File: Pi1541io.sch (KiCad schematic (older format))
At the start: 22 parts, among them J1 IEC1, J2 IEC2, J3 IEC3, J4 ExtSpkr, P1 Conn_02x20_Odd_Even, SW1 SW_Push, SW2 SW_Push, SW3 SW_Push, SW4 SW_Push, SW5 SW_Push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

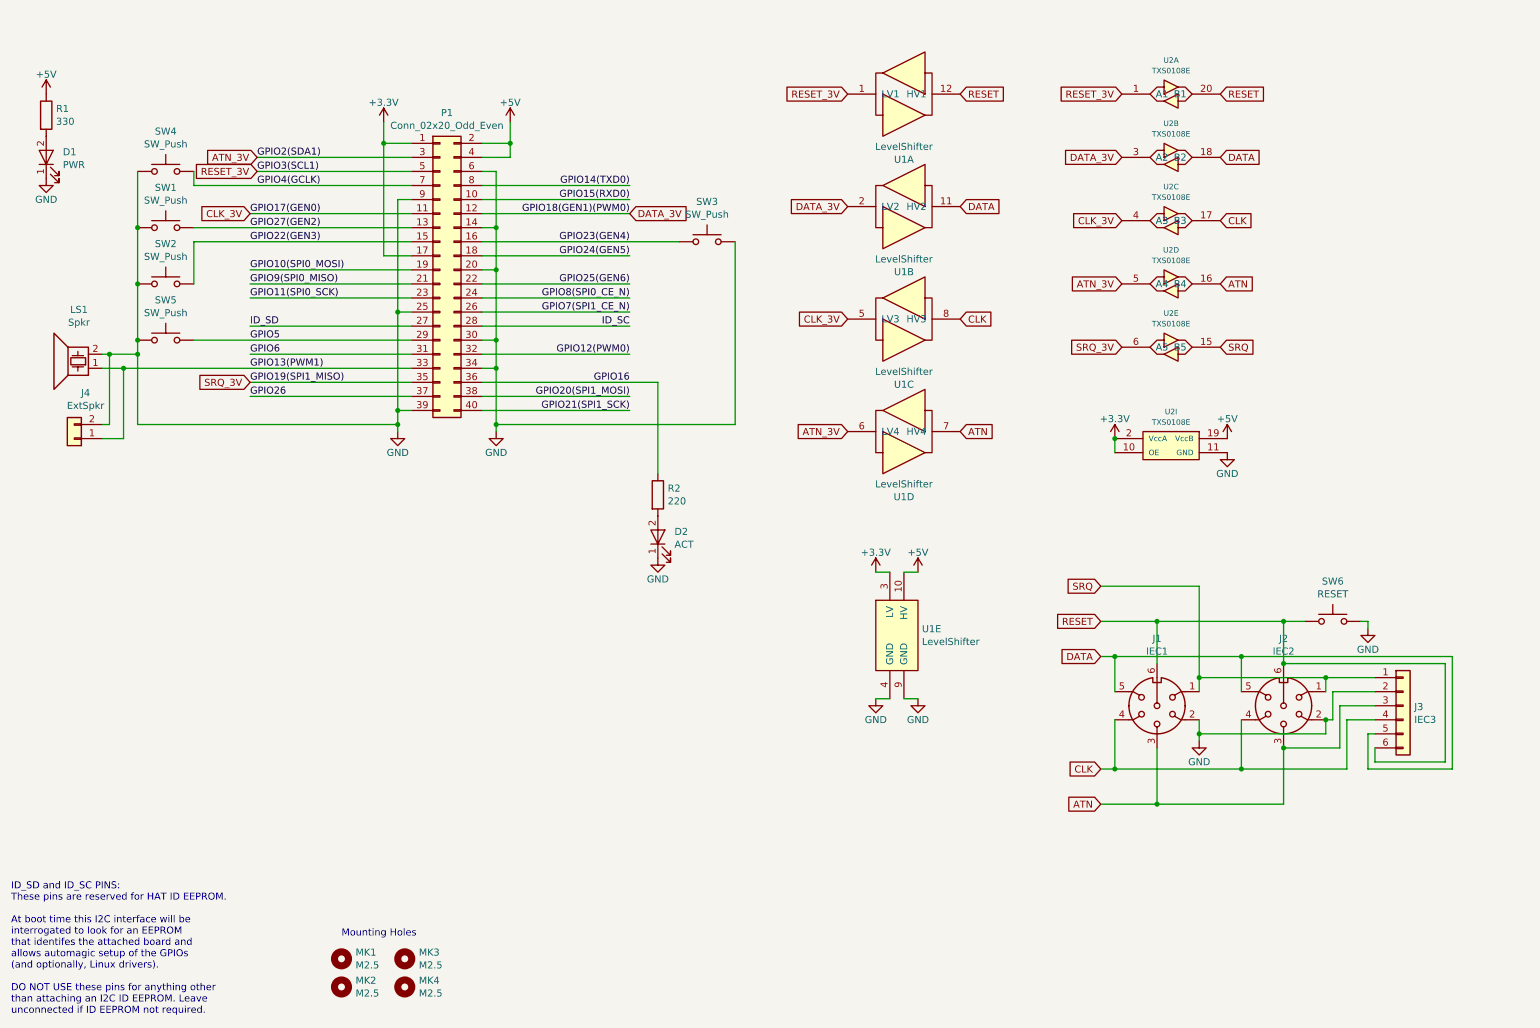
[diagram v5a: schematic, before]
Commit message: Added 7406 driver for outgoing signals.
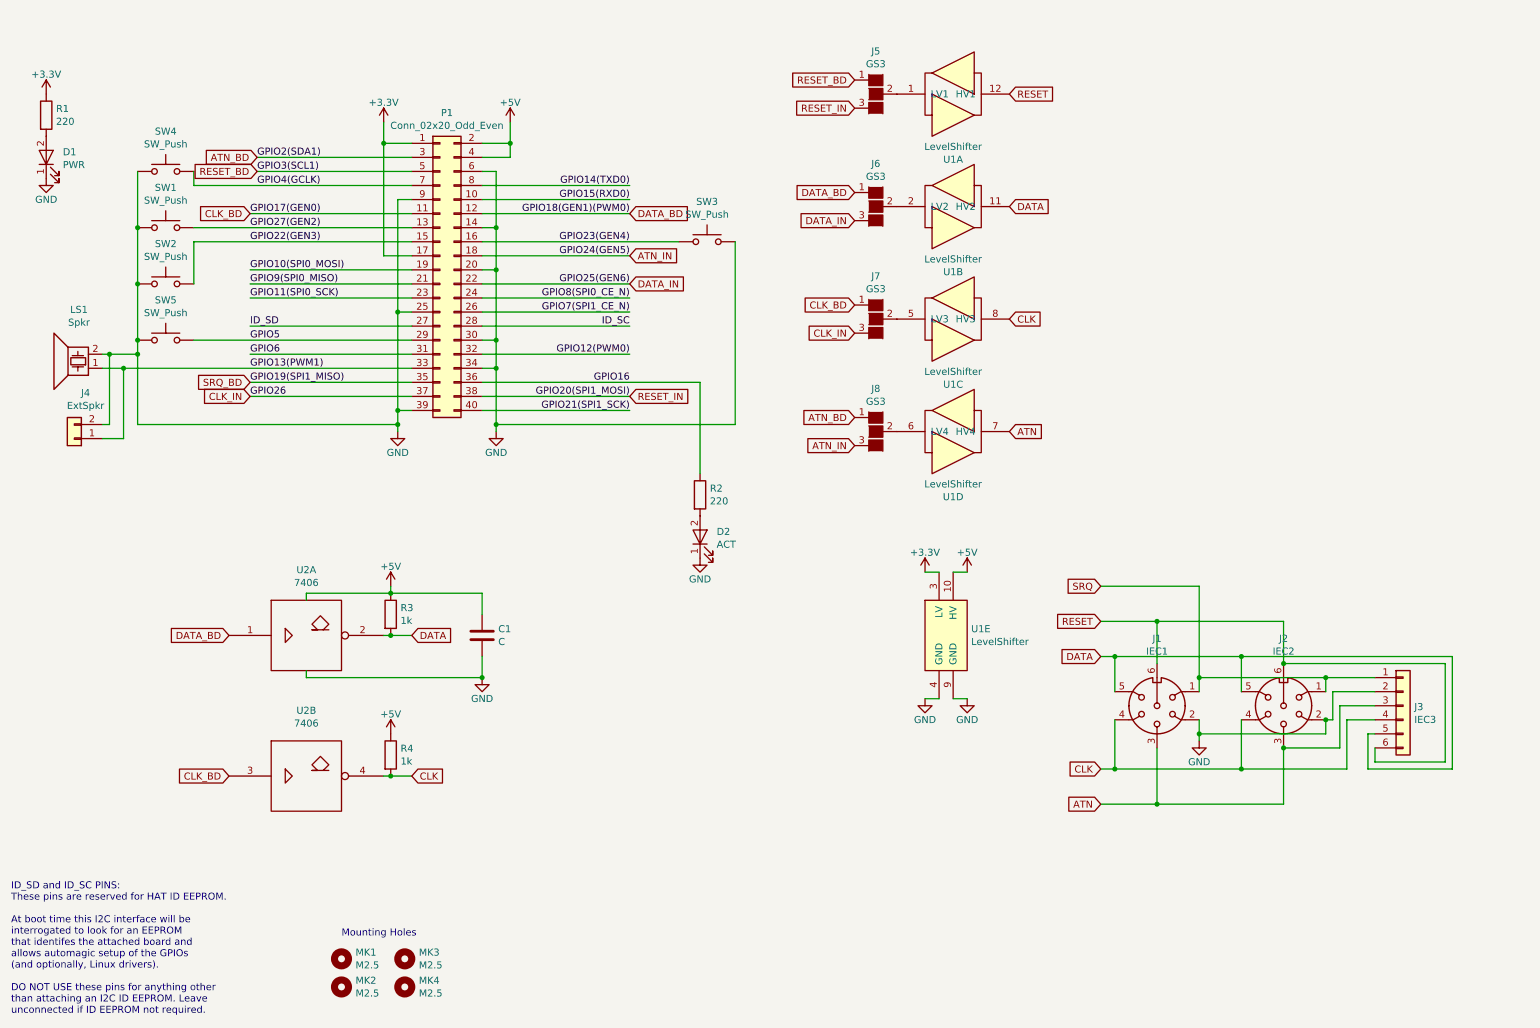
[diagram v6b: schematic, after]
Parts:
- removed SW6: RESET, Buttons_Switches_THT:SW_PUSH_6mm, symbol Switch:SW_Push
- removed U2: TXS0108E, hackup:TXS0108Module, symbol hackup:TXS0108E
- added C1: C, Capacitors_THT:C_Disc_D3.0mm_W1.6mm_P2.50mm, symbol device:C
- added J5, J6, J7, J8: GS3, Connectors:GS3, symbol conn:GS3
- added R3, R4: 1k, Resistors_THT:R_Axial_DIN0207_L6.3mm_D2.5mm_P7.62mm_Horizontal, symbol device:R
- added U2: 7406, Housings_DIP:DIP-14_W7.62mm, symbol Logic_TTL_IEEE:7406
- R1: value 330 -> 220
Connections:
- net +3V3: now also R1.1
- net +5V: now also C1.1, R3.1, R4.1, U2.14 (Vcc), U2.14 (Vcc); no longer R1.1
- net CLK: now also R4.2, U2.4
- net DATA: now also R3.2, U2.2
- net GND: now also C1.2, U2.7 (Gnd), U2.7 (Gnd)
- net ATN_3V: no longer names the net of U1.6 (LV4)
- net ATN_3V: now also J8.2 (G2); no longer P1.3 (Pin_3)
- net CLK_3V: no longer names the net of U1.5 (LV3)
- net CLK_3V: now also J7.2 (G2); no longer P1.11 (Pin_11)
- net DATA_3V: no longer names the net of U1.2 (LV2)
- net DATA_3V: now also J6.2 (G2); no longer P1.12 (Pin_12)
- net GPIO20(SPI1_MOSI) renamed RESET_IN
- net RESET_IN: now also J5.3 (G3)
- net GPIO24(GEN5) renamed ATN_IN
- net ATN_IN: now also J8.3 (G3)
- net GPIO25(GEN6) renamed DATA_IN
- net DATA_IN: now also J6.3 (G3)
- net GPIO26 renamed CLK_IN
- net CLK_IN: now also J7.3 (G3)
- net RESET_3V: no longer names the net of U1.1 (LV1)
- net RESET_3V: now also J5.2 (G2); no longer P1.5 (Pin_5)
- net SRQ_3V renamed SRQ_BD
- new net ATN_BD: J8.1 (G1), P1.3 (Pin_3)
- new net CLK_BD: J7.1 (G1), P1.11 (Pin_11), U2.3
- new net DATA_BD: J6.1 (G1), P1.12 (Pin_12), U2.1
- new net RESET_BD: J5.1 (G1), P1.5 (Pin_5)
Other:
- moved on the sheet: D2, R2, U1A, U1B, U1C, U1D, U1E
